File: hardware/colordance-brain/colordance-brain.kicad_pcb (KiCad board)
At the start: 2 copper layers, 129.5 x 83.5 mm, 130 parts, among them J1 Conn_01x04, J10 RJ45, J11 RJ45, J12 RJ45, J13 RJ45, J14 Anderson, J15 Conn_01x03, J2 Conn_01x03, J3 Conn_01x03, J4 Conn_01x03, J5 Conn_01x03, J6 Conn_01x05, J7 RJ45, J8 RJ45, J9 RJ45, SW1 SW_SPST, U1 74AHCT1G126, U2 74AHCT1G126, U3 Teensy4.1, U4 ISL83490, U5 AM26LS31x, U6 AM26LS31x, U7 AM26LS31x, U8 AP3211

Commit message: Update colordance-brain to 1.3: JLC assembly (completed)
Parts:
- added TH1: PTC 750mA, Fuse:Fuse_1812_4532Metric, B.Cu at (25.6, 64.2)
- C1, C10, C11, C12, C13, C15, C2, C20, C25, C3, C34, C36, C5, C6, C8, C9: value 0.1uF -> 100nF; footprint Capacitor_SMD:C_0603_1608Metric -> Capacitor_SMD:C_0402_1005Metric
- C32: value 10nF -> 100nF; footprint Capacitor_SMD:C_0603_1608Metric -> Capacitor_SMD:C_0402_1005Metric
- D33: footprint Diode_SMD:D_SOD-123 -> Diode_SMD:D_SMA
- D34: value D -> SCHOTTKY; footprint Diode_SMD:D_SOD-323 -> Diode_SMD:D_SMA
- L1: value 5.6uH -> 68uH/2A; footprint Inductor_SMD:L_Taiyo-Yuden_NR-60xx -> Homebrew:L_PROD-Tech_PSPMAA0805
- R11, R4, R5, R8: value 100 -> 470
- R2: value 1.2M -> 120k; footprint Resistor_SMD:R_0805_2012Metric -> Resistor_SMD:R_0603_1608Metric
- R25: value 11.5k -> 2k2
- R26: value 2.21k -> 3k3
- R3: value 330k -> 33k
- U1, U2: footprint Package_TO_SOT_SMD:SOT-353_SC-70-5 -> Package_TO_SOT_SMD:SOT-23-5
- U4: value ISL83490 -> MAX488E
- U8: value AP3211 -> XL1509-5.0E1; footprint Package_TO_SOT_SMD:SOT-23-6 -> Package_SO:SOIC-8_5.23x5.23mm_P1.27mm
- moved R26 53.3 mm to (70.2, 64.2), turned to 0 degrees
- moved R25 50.9 mm to (70.2, 62.6)
- moved D35 17.5 mm to (20.9, 94.6), turned to 180 degrees
- moved D32 17.0 mm to (19.4, 65.0), turned to 180 degrees
- moved D33 15.6 mm to (19.3, 60.6)
- moved C33 10.7 mm to (21.8, 86.4), turned to 180 degrees
- moved C34 8.24 mm to (21.8, 84.8), turned to 180 degrees
- moved C30 6.36 mm to (23.5, 72.9), turned to 180 degrees
- moved D34 6.31 mm to (26.8, 76.4), turned to 180 degrees
- moved D1 5.71 mm to (29.8, 90.5), turned to 0 degrees
- moved L1 5.54 mm to (31.2, 83.4)
- moved R1 4.71 mm to (29.8, 92.2)
- moved C32 4.48 mm to (22.0, 77.8), turned to 180 degrees
- moved C31 3.26 mm to (21.5, 76.2)
- moved U8 2.11 mm to (21.9, 81.3), turned to 180 degrees
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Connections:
- C13 pad 1: +3V3 -> +5V
- C32 pad 1: Net-(C32-Pad1) -> +12V
- C32 pad 2: Net-(C32-Pad2) -> GND
- D33 pad 1: Net-(C32-Pad2) -> +12V
- D34 pad 1: Net-(C32-Pad1) -> Net-(D34-K)
- D34 pad 2: +5V -> GND
- J14 pad 1: +12V -> Net-(J14-Pad1)
- L1 pad 1: Net-(C32-Pad2) -> Net-(D34-K)
- R25 pad 1: +5V -> Net-(U4-RO)
- R25 pad 2: Net-(R25-Pad2) -> /INTERFACE_IN
- R26 pad 1: Net-(R25-Pad2) -> /INTERFACE_IN
- U4 pad 1: +3V3 -> +5V
- U4 pad 2: /INTERFACE_IN -> Net-(U4-RO)
- U8 pad 1: Net-(C32-Pad1) -> +12V
- U8 pad 2: GND -> Net-(D34-K)
- U8 pad 3: Net-(R25-Pad2) -> +5V
- U8 pad 4: +12V -> GND
- U8 pad 5: +12V -> GND
- U8 pad 6: Net-(C32-Pad2) -> GND
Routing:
- net +5V: track 427.3 -> 450.4 mm, vias 6 -> 9
- net +3V3: track 97.1 -> 76.3 mm
- net Net-(C32-Pad2): track 11.0 -> 0.00 mm
- net Net-(D34-K): track 0.00 -> 10.5 mm
- net +12V: track 43.0 -> 53.3 mm, vias 0 -> 1
- net GND: track 276.8 -> 267.9 mm, vias 57 -> 80
- net Net-(J14-Pad1): track 0.00 -> 5.99 mm
- net Net-(C32-Pad1): track 4.17 -> 0.00 mm
- net Net-(R25-Pad2): track 3.87 -> 0.00 mm
- net /INTERFACE_IN: track 17.3 -> 14.6 mm, vias 2 -> 0
- net Net-(U4-RO): track 0.00 -> 2.19 mm
- net /AUX_SERIAL_IN: track 11.3 -> 9.81 mm
- net /sheet6087FA83/LED2_Y: track 24.5 -> 23.2 mm
- net Net-(D1-K): track 3.44 -> 2.37 mm
- net /sheet6087EBF5/LED3_Z: track 12.6 -> 11.6 mm
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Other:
- board text added: "+"
- board text added: "-"
- board text added: "TEENSY 4.1"
- board text added: "colordance-brain v1.3"
- board text removed: "colordance-brain v1.2"

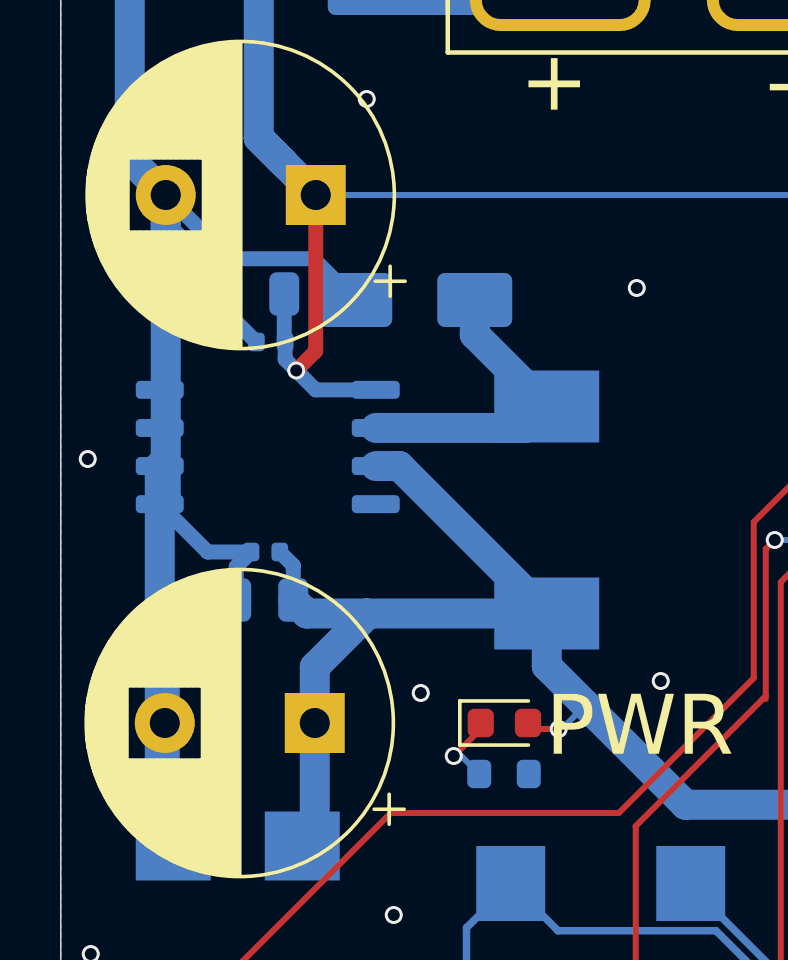
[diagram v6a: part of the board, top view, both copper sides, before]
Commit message: Fix colordance-brain v1.3 footprint for XL1509 SMPS
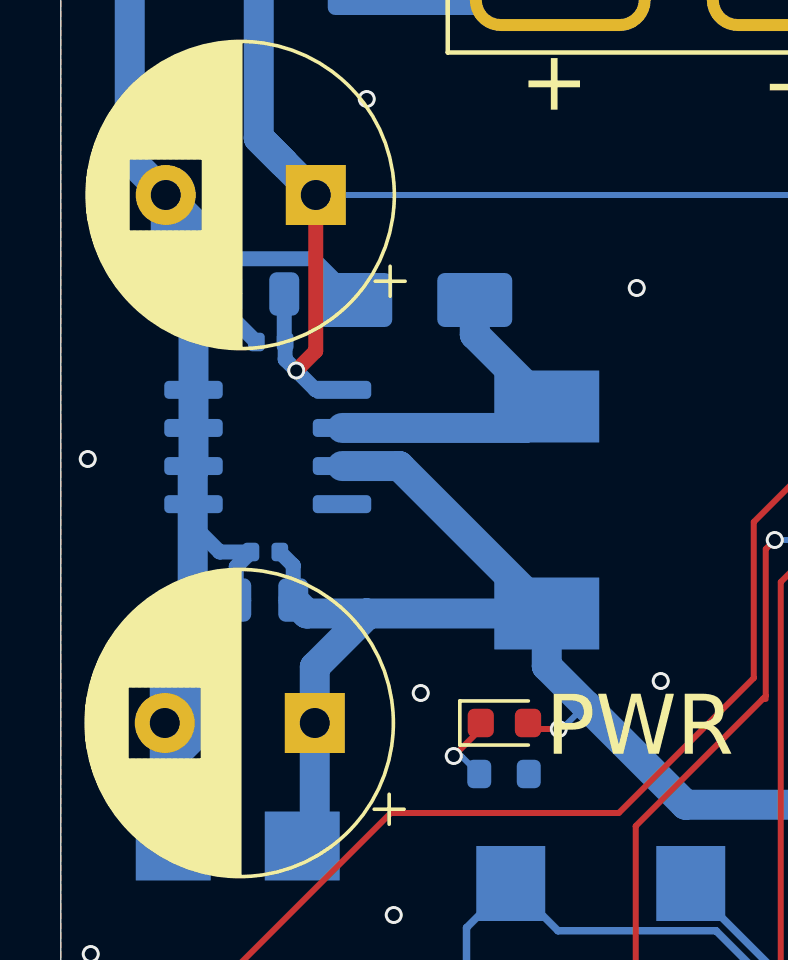
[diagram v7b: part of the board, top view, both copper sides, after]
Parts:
- U8: footprint Package_SO:SOIC-8_5.23x5.23mm_P1.27mm -> Package_SO:SOIC-8_3.9x4.9mm_P1.27mm
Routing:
- net GND: track 267.9 -> 266.0 mm
- net +5V: track 450.4 -> 451.6 mm
- net Net-(D34-K): track 10.5 -> 11.7 mm
- net +12V: track 53.3 -> 52.1 mm
